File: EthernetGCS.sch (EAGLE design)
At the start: 19 parts, among them U1 MIC5219-3.3V, U3 FT232RL-BASICSSOP, X1 USB-A-H

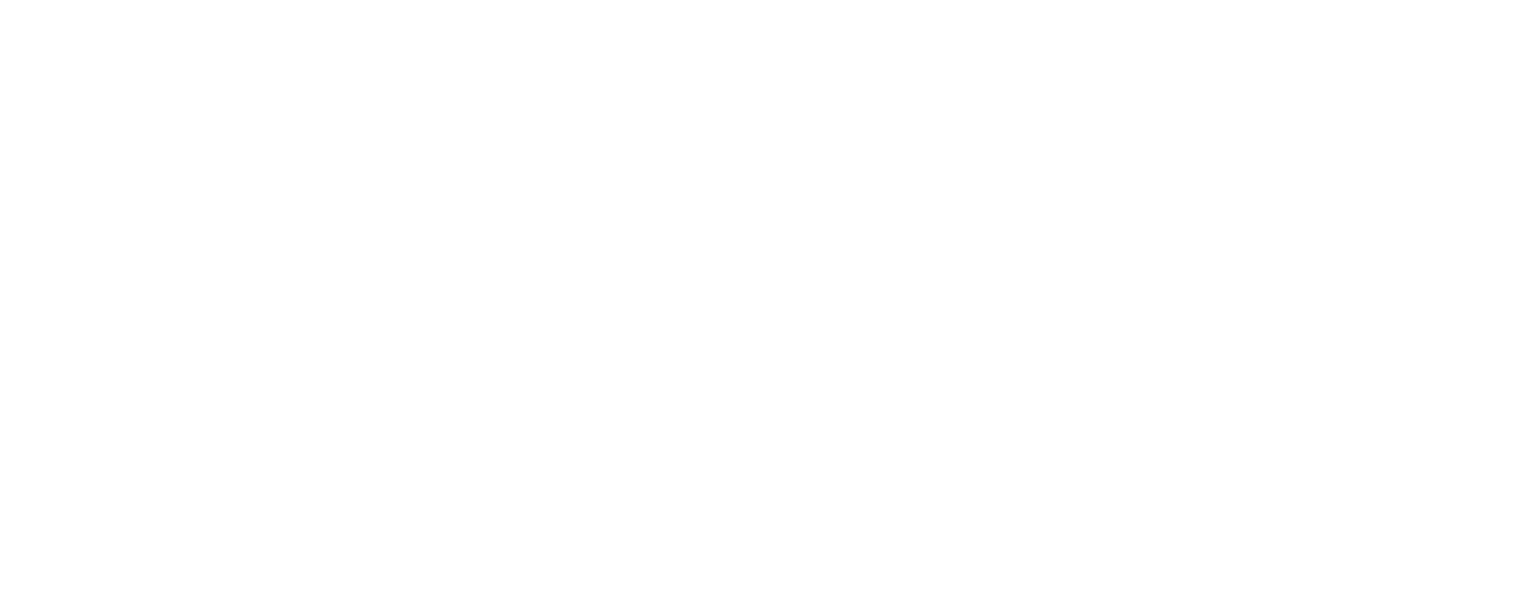
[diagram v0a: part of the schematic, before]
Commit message: Adding Ethernet IC, a PIC 24F and a RJ45 connector.
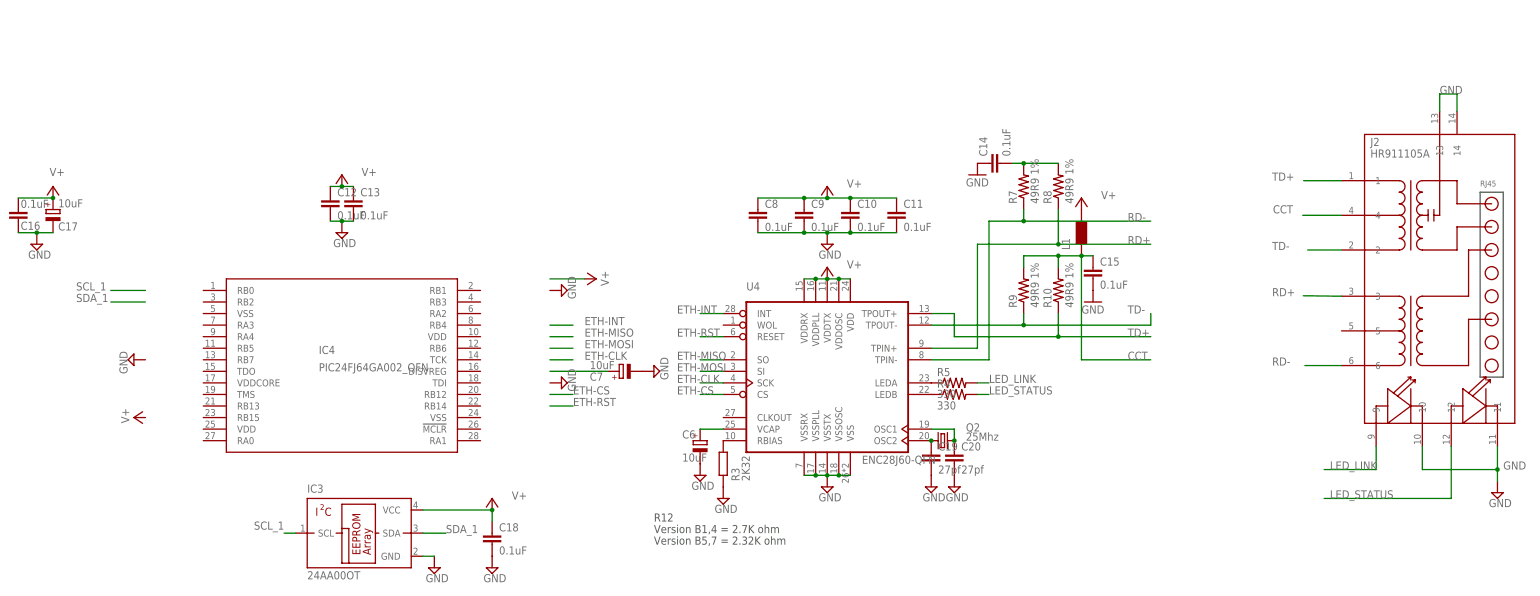
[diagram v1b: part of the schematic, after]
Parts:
- added C10, C11, C12, C13, C14, C15, C18, C8, C9: 0.1uF, SparkFun:CAP0402-CAP
- added C16: 0.1uF, rcl:C-EUC0805
- added C17, C6, C7: 10uF, rcl:CPOL-EUSMCA
- added C19, C20: 27pf, SparkFun:CAP0402-CAP
- added IC3: 24AA00OT, microchip:24AA00OT
- added IC4: PIC24FJ64GA002_QFN, microchip:PIC24FJ64GA002_QFN
- added J2: HR911105A, CONNECTER:HR911105A
- added L1: (no value), wuerth-elektronik:WE-KIL_0805
- added Q2: 25Mhz, crystal:CRYSTALCTS406
- added R10, R7, R8, R9: 49R9 1%, SparkFun:RESISTOR0402-RES
- added R3: 2K32, rcl:R-EU_R0805
- added R4, R5: 330, SparkFun:RESISTOR0402-RES
- added U4: ENC28J60-QFN, microchip-enc28j60:ENC28J60-QFN
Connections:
- new net CCT: C15.1, J2.4, L1.1, R10.2, R9.2
- new net ETH-CLK: U4.SCK
- new net ETH-CS: U4.CS
- new net ETH-INT: U4.INT
- new net ETH-MISO: U4.SO
- new net ETH-MOSI: U4.SI
- new net ETH-RST: U4.RESET
- new net LED_LINK: J2.9, R5.2
- new net LED_STATUS: J2.12, R4.2
- new net N$13: C6.+, U4.VCAP
- new net N$14: C19.1, Q2.1, U4.OSC2
- new net N$15: C20.1, Q2.2, U4.OSC1
- new net N$16: C7.+
- new net N$17: R3.2, U4.RBIAS
- new net N$18: R5.1, U4.LEDA
- new net N$19: R4.1, U4.LEDB
- new net N$22: C14.2, R7.2, R8.2
- new net RD+: J2.3, R8.1, U4.TPIN+
- new net RD-: J2.6, R7.1, U4.TPIN-
- new net SCL_1: IC3.SCL
- new net SDA_1: IC3.SDA
- new net TD+: J2.1, R10.1, U4.TPOUT+
- new net TD-: J2.2, R9.1, U4.TPOUT-
- new net V+: C10.1, C11.1, C12.1, C13.1, C16.1, C17.+, C18.1, C8.1, C9.1, IC3.VCC, L1.2, U4.VDD, U4.VDDOSC, U4.VDDPLL, U4.VDDRX, U4.VDDTX
- net GND: now also C10.2, C11.2, C12.2, C13.2, C14.1, C15.2, C16.2, C17.-, C18.2, C19.2, C20.2, C6.-, C7.-, C8.2, C9.2, IC3.GND, J2.10, J2.11, J2.13, J2.14, R3.1, U4.VSS, U4.VSSOSC, U4.VSSPLL, U4.VSSRX, U4.VSSTX
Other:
- note added: "R12"
- note added: "Version B1,4 = 2.7K ohm"
- note added: "Version B5,7 = 2.32K ohm"

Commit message: Cloning 3DR board, to use as reference.
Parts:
- removed C4, C5: 0.1uF, SparkFun:CAP0402-CAP
- removed L6: BKP1005HS121-T, pel_dipol_comp:INDUCTOR-0402
- removed U3: FT232RL-BASICSSOP, SparkFun:FT232RL-BASICSSOP
- removed X1: USB-A-H, SparkFun:USB-A-H
- added C21: 1uF, SparkFun:CAP0402-CAP
- added C22: 470pF, SparkFun:CAP0402-CAP
- added C23: 10uF, SparkFun:CAP_POL1206
- added C24, C25: 0.1uF, SparkFun:CAP0402-CAP
- added J$2: SMA_EDGE, 3DRobotics:SMA_EDGE
- added JP3, JP4: FIDUCIAL1X2, SparkFun:FIDUCIAL1X2
- added JP5, JP6: (no value), pinhead:PINHD-1X3
- added L2, L3: BLM15HD102SN1, pel_dipol_comp:INDUCTOR-0402
- added L7: BKP1005HS121-T, pel_dipol_comp:INDUCTOR-0402
- added LED3: GREEN, SparkFun:LED0603
- added LED4: RED, SparkFun:LED0603
- added R11, R6: 330, SparkFun:RESISTOR0402-RES
- added U5: MIC5219-3.3V, SparkFun:V_REG_LDOSMD
- added U6: (no value), 3DRobotics:HM-TRPSMD
- added U7: FT232RL-BASICSSOP, SparkFun:FT232RL-BASICSSOP
- added X2: USB-A-H, SparkFun:USB-A-H
- JP1: value FIDUCIAL1X2 -> (none); device SparkFun:FIDUCIAL1X2 -> pinhead:PINHD-1X3
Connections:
- removed net DTR: U3.DTR
- removed net N$12: L6.1, X1.GND
- removed net N$3: C4.1, U3.3V3OUT, U3.VCCIO
- removed net N$5: U3.USBDP, X1.D-
- removed net N$6: U3.USBDM, X1.D+
- new net CTS1: U6.!CONFIG, U7.CTS
- new net DTR1: U7.DTR
- new net N$20: C22.1, U5.BP
- new net N$21: J$2.SIGNAL, U6.ANT
- new net N$23: C24.1, U7.3V3OUT, U7.VCCIO
- new net N$24: U7.USBDP, X2.D-
- new net N$25: U7.USBDM, X2.D+
- new net N$26: LED4.A, R11.1
- new net N$27: LED3.A, R6.1
- new net N$28: LED4.C, U7.TXLED
- new net N$29: LED3.C, U7.RXLED
- new net N$30: L2.2, U6.DTX
- new net N$31: L3.2, U6.DRX
- new net N$32: L7.1, X2.GND
- new net RTS1: U6.!ENABLE, U7.RTS
- new net RX1: L3.1, U7.TXD
- new net TX1: L2.1, U7.RXD
- net 3.3V: now also C23.+, U5.OUT, U6.VCC
- net 5V: now also C21.1, C25.1, L7.2, R11.2, R6.2, U5.EN, U5.IN, U7.VCC; no longer C5.1, L6.2, U3.VCC
- net CTS: no longer U3.CTS
- net GND: now also C21.2, C22.2, C23.-, C24.2, C25.2, J$2.GND@0, J$2.GND@1, J$2.GND@2, J$2.GND@3, U5.GND, U6.AGND, U6.GND, U7.AGND, U7.GND1, U7.GND2, U7.GND3, U7.TEST, X2.VBUS; no longer C4.2, C5.2, U3.AGND, U3.GND1, U3.GND2, U3.GND3, U3.TEST, X1.VBUS
- net N$10: no longer U3.TXLED
- net N$11: no longer U3.RXLED
- net RTS: no longer U3.RTS
- net RX: no longer U3.TXD
- net TX: no longer U3.RXD
